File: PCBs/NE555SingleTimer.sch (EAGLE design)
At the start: 5 parts, among them IC1 LM555N

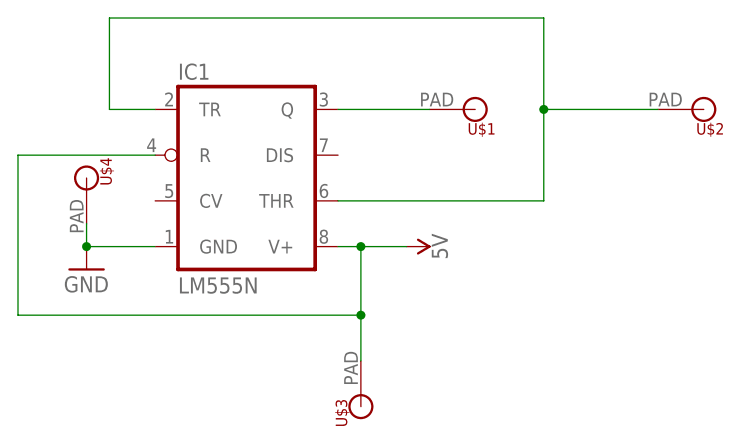
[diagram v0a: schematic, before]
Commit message: Update for Dim width is 42 length is 28 for type 2 pcb
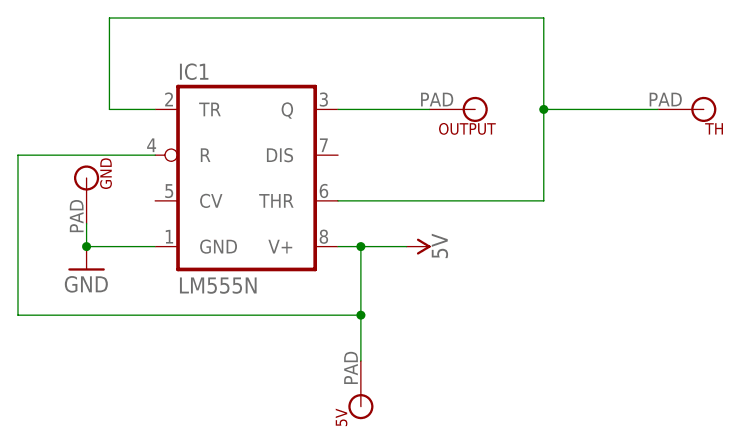
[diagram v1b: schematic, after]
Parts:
- renumbered U$1 to OUTPUT, U$2 to TH, U$3 to 5V, U$4 to GND
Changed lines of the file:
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@@
 <parts>
 <part name="IC1" library="linear" library_urn="urn:adsk.eagle:library:262" deviceset="*555" device="N" package3d_urn="urn:adsk.eagle:package:16409/2" technology="LM"/>
-<part name="U$1" library="microbit" deviceset="MICROBIT_PAD" device=""/>
-<part name="U$2" library="microbit" deviceset="MICROBIT_PAD" device=""/>
-<part name="U$3" library="microbit" deviceset="MICROBIT_PAD" device=""/>
-<part name="U$4" library="microbit" deviceset="MICROBIT_PAD" device=""/>
+<part name="OUTPUT" library="microbit" deviceset="MICROBIT_PAD" device=""/>
+<part name="TH" library="microbit" deviceset="MICROBIT_PAD" device=""/>
+<part name="5V" library="microbit" deviceset="MICROBIT_PAD" device=""/>
+<part name="GND" library="microbit" deviceset="MICROBIT_PAD" device=""/>
 <part name="SUPPLY1" library="SparkFun-PowerSymbols" library_urn="urn:adsk.eagle:library:530" deviceset="5V" device=""/>
 <part name="GND1" library="supply1" library_urn="urn:adsk.eagle:library:371" deviceset="GND" device=""/>
@@
 <attribute name="VALUE" x="53.34" y="43.053" size="1.778" layer="96"/>
 </instance>
-<instance part="U$1" gate="G$1" x="86.36" y="63.5" smashed="yes" rot="R180">
+<instance part="OUTPUT" gate="G$1" x="86.36" y="63.5" smashed="yes" rot="R180">
 <attribute name="NAME" x="88.646" y="61.976" size="1.27" layer="94" rot="R180"/>
 </instance>
-<instance part="U$2" gate="G$1" x="111.76" y="63.5" smashed="yes" rot="R180">
+<instance part="TH" gate="G$1" x="111.76" y="63.5" smashed="yes" rot="R180">
 <attribute name="NAME" x="114.046" y="61.976" size="1.27" layer="94" rot="R180"/>
 </instance>
-<instance part="U$3" gate="G$1" x="73.66" y="30.48" smashed="yes" rot="R90">
+<instance part="5V" gate="G$1" x="73.66" y="30.48" smashed="yes" rot="R90">
 <attribute name="NAME" x="72.136" y="28.194" size="1.27" layer="94" rot="R90"/>
 </instance>
-<instance part="U$4" gate="G$1" x="43.18" y="55.88" smashed="yes" rot="R270">
+<instance part="GND" gate="G$1" x="43.18" y="55.88" smashed="yes" rot="R270">
 <attribute name="NAME" x="44.704" y="58.166" size="1.27" layer="94" rot="R270"/>
 </instance>
@@
 <wire x1="73.66" y1="40.64" x2="73.66" y2="48.26" width="0.1524" layer="91"/>
 <junction x="73.66" y="48.26"/>
-<pinref part="U$3" gate="G$1" pin="P$1"/>
+<pinref part="5V" gate="G$1" pin="P$1"/>
 <wire x1="73.66" y1="35.56" x2="73.66" y2="40.64" width="0.1524" layer="91"/>
 <junction x="73.66" y="40.64"/>
@@
 <segment>
 <pinref part="IC1" gate="A" pin="Q"/>
-<pinref part="U$1" gate="G$1" pin="P$1"/>
+<pinref part="OUTPUT" gate="G$1" pin="P$1"/>
 <wire x1="71.12" y1="63.5" x2="81.28" y2="63.5" width="0.1524" layer="91"/>
 </segment>
@@
 <pinref part="IC1" gate="A" pin="TR"/>
 <wire x1="45.72" y1="63.5" x2="50.8" y2="63.5" width="0.1524" layer="91"/>
-<pinref part="U$2" gate="G$1" pin="P$1"/>
+<pinref part="TH" gate="G$1" pin="P$1"/>
 <wire x1="106.68" y1="63.5" x2="93.98" y2="63.5" width="0.1524" layer="91"/>
 <junction x="93.98" y="63.5"/>
@@
 <pinref part="GND1" gate="1" pin="GND"/>
 <wire x1="50.8" y1="48.26" x2="43.18" y2="48.26" width="0.1524" layer="91"/>
-<pinref part="U$4" gate="G$1" pin="P$1"/>
+<pinref part="GND" gate="G$1" pin="P$1"/>
 <wire x1="43.18" y1="50.8" x2="43.18" y2="48.26" width="0.1524" layer="91"/>
 <junction x="43.18" y="48.26"/>
